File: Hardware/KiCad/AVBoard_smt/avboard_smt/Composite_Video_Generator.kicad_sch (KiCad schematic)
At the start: 47 parts, among them IC36 4040N, IC37 7430N, IC39 7400N, IC40 4040N, IC41 7400N, IC43 7400N, IC44 7486N, IC45 7400N, IC46 74257N, IC47 74257N, IC48 74564N, IC53 7404N, J2 VID_TO_MOBO, U2 THS7374

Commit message: update kicad SMT BOMs
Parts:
- V.RAM.0: MPN CONN SOCKET PLCC 68POS TIN -> 8468-21B1-RK-TR
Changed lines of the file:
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@@
       (effects (font (size 1.27 1.27)) hide)
     )
-    (property "MPN" "CONN SOCKET PLCC 68POS TIN" (at -330.2 154.94 0)
+    (property "MPN" "8468-21B1-RK-TR" (at -330.2 154.94 0)
       (effects (font (size 1.27 1.27)) hide)
     )
@@
       (effects (font (size 1.27 1.27)) hide)
     )
-    (property "MPN" "CONN SOCKET PLCC 68POS TIN" (at 106.68 132.08 0)
+    (property "MPN" "8468-21B1-RK-TR" (at 106.68 132.08 0)
       (effects (font (size 1.27 1.27)) hide)
     )
@@
       (effects (font (size 1.27 1.27)) hide)
     )
-    (property "MPN" "CONN SOCKET PLCC 68POS TIN" (at 314.96 172.72 0)
+    (property "MPN" "8468-21B1-RK-TR" (at 314.96 172.72 0)
       (effects (font (size 1.27 1.27)) hide)
     )
@@
       (effects (font (size 1.27 1.27)) hide)
     )
-    (property "MPN" "CONN SOCKET PLCC 68POS TIN" (at 88.9 332.74 0)
-      (effects (font (size 1.27 1.27)) hide)
-    )
+    (property "MPN" "8468-21B1-RK-TR" (at 88.9 332.74 0)
+      (effects (font (size 1.27 1.27)) hide)
+    )

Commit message: collect production documents for quoting
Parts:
- J2: footprint Connector_FFC-FPC:TE_4-1734839-0_1x40-1MP_P0.5mm_Horizontal -> SamacSys_Parts:F34G1A7Q1E8C40; MPN 4-1734839-0 -> F34G-1A7Q1-E8C40

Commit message: replace dual ported frame buffer with mirrored single ported rams
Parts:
- removed V.RAM.0: PDPRAM_32K_V2, Package_LCC:PLCC-68_SMD-Socket, symbol signals-eagle-import:PDPRAM_32K_V2
- added IC1, IC9: AS7C256A-10TIN, SOP55P1340X120-28N, symbol SamacSys_Parts:AS7C256A-10TIN
- added IC2_AUD0: 7432N, Package_SO:TSSOP-14_4.4x5mm_P0.65mm, symbol signals-eagle-import:7432N
- added U3, U4, U5: 74AHC373, Package_SO:TSSOP-20_4.4x6.5mm_P0.65mm, symbol 74xx:74AHC373
- added U6: 74AC00, Package_SO:TSSOP-14_4.4x5mm_P0.65mm, symbol 74xx:7400
- added U7: 74VHC74, Package_SO:TSSOP-14_4.4x5mm_P0.65mm, symbol 74xx:74HC74
- added U8, U9: 74HC244, Package_SO:TSSOP-20_4.4x6.5mm_P0.65mm, symbol 74xx:74HCT244
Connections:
- net CLK14: now also U7.2 (D)
- net CLK28: now also U7.11 (C), U7.3 (C)
- net CLK7: now also U6.1, U6.2
- net GND: now also IC1.21 (GND), IC1.27 (~{CE}), IC9.21 (GND), IC9.27 (~{CE}), U3.10 (GND), U4.10 (GND), U5.10 (GND), U6.7 (GND), U7.7 (GND), U8.10 (GND), U9.10 (GND)
- net P0: now also IC1.26 (I/O7), U3.19 (O7)
- net P1: now also IC1.25 (I/O6), U3.16 (O6)
- net P2: now also IC1.24 (I/O5), U3.15 (O5)
- net P3: now also IC1.23 (I/O4), U3.12 (O4)
- net P4: now also IC1.22 (I/O3), U3.9 (O3)
- net P5: now also IC1.20 (I/O2), U3.6 (O2)
- net P6: now also IC1.19 (I/O1), U3.5 (O1)
- net P7: now also IC1.18 (I/O0), U3.2 (O0)
- net VA0: now also IC9.17 (A0), U4.3 (D0)
- net VA1: now also IC9.16 (A1), U4.4 (D1)
- net VA10: now also IC9.28 (A10), U5.8 (D3)
- net VA11: now also IC9.2 (A11), U5.13 (D4)
- net VA12: now also IC9.9 (A12), U5.14 (D5)
- net VA13: now also IC9.5 (A13), U5.17 (D6)
- net VA14: now also IC9.8 (A14), U5.18 (D7)
- net VA2: now also IC9.15 (A2), U4.7 (D2)
- net VA3: now also IC9.14 (A3), U4.8 (D3)
- net VA4: now also IC9.13 (A4), U4.13 (D4)
- net VA5: now also IC9.12 (A5), U4.14 (D5)
- net VA6: now also IC9.11 (A6), U4.17 (D6)
- net VA7: now also IC9.10 (A7), U5.3 (D0)
- net VA8: now also IC9.4 (A8), U5.4 (D1)
- net VA9: now also IC9.3 (A9), U5.7 (D2)
- net VCC: now also IC1.7 (VCC), IC9.7 (VCC), U3.20 (VCC), U4.20 (VCC), U5.20 (VCC), U6.14 (VCC), U7.1 (~{R}), U7.10 (~{S}), U7.13 (~{R}), U7.14 (VCC), U7.4 (~{S}), U8.20 (VCC), U9.20 (VCC)
- net VD0: now also IC9.18 (I/O0), U3.3 (D0)
- net VD1: now also IC9.19 (I/O1), U3.4 (D1)
- net VD2: now also IC9.20 (I/O2), U3.7 (D2)
- net VD3: now also IC9.22 (I/O3), U3.8 (D3)
- net VD4: now also IC9.23 (I/O4), U3.13 (D4)
- net VD5: now also IC9.24 (I/O5), U3.14 (D5)
- net VD6: now also IC9.25 (I/O6), U3.17 (D6)
- net VD7: now also IC9.26 (I/O7), U3.18 (D7)
- net VIDPAGE: now also U9.11 (2A3)
- net XCLK: now also U6.4
- net ~{VOE}: now also IC9.1 (~{OE})
- net ~{VWE}: now also IC53.11 (I), IC9.6 (~{WE})
- net PIXLATCH: now reaches COL_CTR0.9 (Q1), IC48.11 (CLK)
- net PIXLATCH: now also U6.5, U7.12 (D)
- net PAY6: now reaches ROW_CTR0.4 (Q7)
- net PAY6: now also U9.13 (2A2)
- net PAY5: now reaches ROW_CTR0.2 (Q6)
- net PAY5: now also U9.15 (2A1)
- net PAY4: now reaches ROW_CTR0.3 (Q5)
- net PAY4: now also U9.17 (2A0)
- net PAY3: now reaches ROW_CTR0.5 (Q4)
- net PAY3: now also U9.8 (1A3)
- net PAY2: now reaches ROW_CTR0.6 (Q3)
- net PAY2: now also U9.6 (1A2)
- net PAY1: now reaches ROW_CTR0.7 (Q2)
- net PAY1: now also U9.4 (1A1)
- net PAY0: now reaches ROW_CTR0.9 (Q1)
- net PAY0: now also U9.2 (1A0)
- net PAX6: now reaches COL_CTR0.13 (Q8)
- net PAX6: now also U8.13 (2A2)
- net PAX5: now reaches COL_CTR0.4 (Q7)
- net PAX5: now also U8.15 (2A1)
- net PAX4: now reaches COL_CTR0.2 (Q6)
- net PAX4: now also U8.17 (2A0)
- net PAX3: now reaches COL_CTR0.3 (Q5)
- net PAX3: now also U8.8 (1A3)
- net PAX2: now reaches COL_CTR0.5 (Q4)
- net PAX2: now also U8.6 (1A2)
- net PAX1: now reaches COL_CTR0.6 (Q3)
- net PAX1: now also U8.4 (1A1)
- net PAX0: now reaches COL_CTR0.7 (Q2)
- net PAX0: now also U8.2 (1A0)
- new net: U6.10, U6.6, U6.9
- new net: IC1.1 (~{OE}), U7.9 (Q), U8.1 (1OE), U8.19 (2OE), U9.1 (1OE), U9.19 (2OE)
- new net: U6.12, U6.3
- new net: U6.13, U6.8
- new net LAG14: IC2_AUD0.12 (I0), U7.5 (Q)
- new net MA0: IC1.17 (A0), U4.2 (O0), U8.18 (1Y0)
- new net MA1: IC1.16 (A1), U4.5 (O1), U8.16 (1Y1)
- new net MA10: IC1.28 (A10), U5.9 (O3), U9.12 (1Y3)
- new net MA11: IC1.2 (A11), U5.12 (O4), U9.3 (2Y0)
- new net MA12: IC1.9 (A12), U5.15 (O5), U9.5 (2Y1)
- new net MA13: IC1.5 (A13), U5.16 (O6), U9.7 (2Y2)
- new net MA14: IC1.8 (A14), U5.19 (O7), U9.9 (2Y3)
- new net MA2: IC1.15 (A2), U4.6 (O2), U8.14 (1Y2)
- new net MA3: IC1.14 (A3), U4.9 (O3), U8.12 (1Y3)
- new net MA4: IC1.13 (A4), U4.12 (O4), U8.3 (2Y0)
- new net MA5: IC1.12 (A5), U4.15 (O5), U8.5 (2Y1)
- new net MA6: IC1.11 (A6), U4.16 (O6), U8.7 (2Y2)
- new net MA7: IC1.10 (A7), U5.2 (O0), U9.18 (1Y0)
- new net MA8: IC1.4 (A8), U5.5 (O1), U9.16 (1Y1)
- new net MA9: IC1.3 (A9), U5.6 (O2), U9.14 (1Y2)
- new net VWE: IC53.10 (O), U3.11 (LE), U4.11 (LE), U5.11 (LE)
- new net ~{MirrorLoad}: IC2_AUD0.13 (I1), U3.1 (OE), U4.1 (OE), U5.1 (OE), U6.11
- new net ~{MirrorWE}: IC1.6 (~{WE}), IC2_AUD0.11 (O)
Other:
- note added: "BLITSIDE FRAMEBUFFER"
- note added: "VIDSIDE FRAMEBUFFER MIRROR"
- moved on the sheet: COL_CTR0B, IC36B, IC40B, IC53E, ROW_CTR0B

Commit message: design out the 4K dualport ram
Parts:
- IC1, IC9: MPN (none) -> AS7C256A-10TIN; Manufacturer_Part_Number AS7C256A-10TIN -> (none)
- U3, U4, U5: MPN (none) -> 74VHC373MTCX

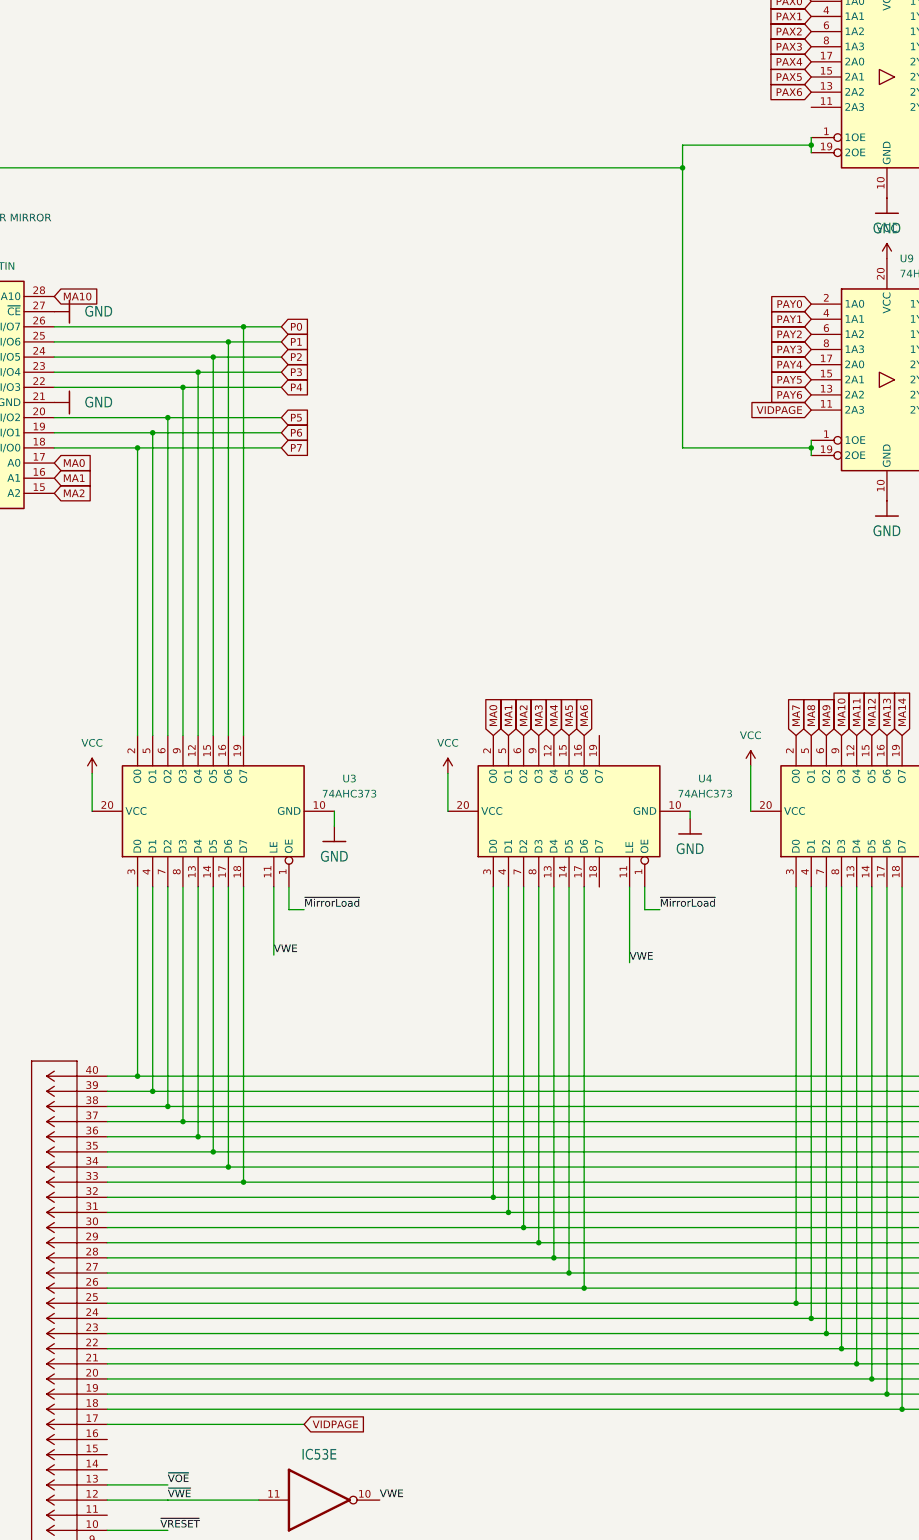
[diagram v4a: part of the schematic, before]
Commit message: connect loose unused inputs to ground
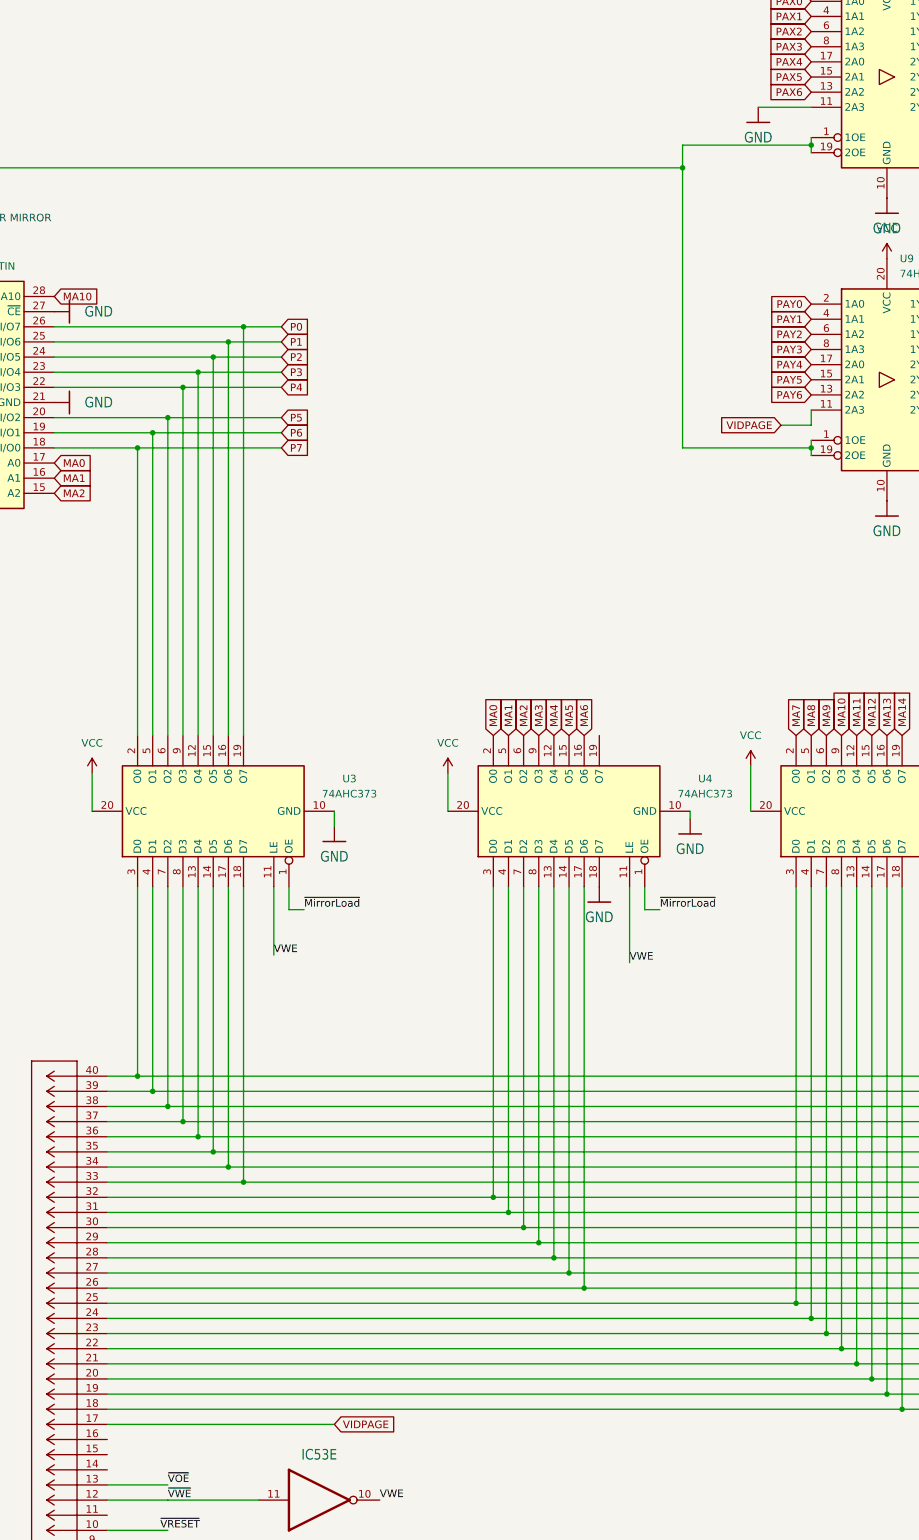
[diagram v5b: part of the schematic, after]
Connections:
- net GND: now also U4.18 (D7), U8.11 (2A3)

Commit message: fix composite video generator board
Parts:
- removed IC2_AUD0: 7432N, Package_SO:TSSOP-14_4.4x5mm_P0.65mm, symbol signals-eagle-import:7432N
- removed U6: 74AC00, Package_SO:TSSOP-14_4.4x5mm_P0.65mm, symbol 74xx:7400
- removed U7: 74VHC74, Package_SO:TSSOP-14_4.4x5mm_P0.65mm, symbol 74xx:74HC74
- added unit 1 of IC53
- added MIRROR_OR: 7432N, Package_SO:TSSOP-14_4.4x5mm_P0.65mm, symbol signals-eagle-import:7432N
- added PIX_CLK_DELAY: 74164N, Package_SO:TSSOP-14_4.4x5mm_P0.65mm, symbol signals-eagle-import:74164N
- SCAN_DELAY0, X_SCALER0: MPN MC74HC161ADTR2G -> SN74HC161PWR
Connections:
- net CLK14: now also MIRROR_OR.1 (I0)
- net CLK28: now also PIX_CLK_DELAY.8 (CLK)
- net GND: now also MIRROR_OR.7 (GND), PIX_CLK_DELAY.7 (GND)
- net P0: now also IC1.18 (I/O0), U3.2 (O0); no longer IC1.26 (I/O7), U3.19 (O7)
- net P1: now also IC1.19 (I/O1), U3.5 (O1); no longer IC1.25 (I/O6), U3.16 (O6)
- net P2: now also IC1.20 (I/O2), U3.6 (O2); no longer IC1.24 (I/O5), U3.15 (O5)
- net P3: now also IC1.22 (I/O3), U3.9 (O3); no longer IC1.23 (I/O4), U3.12 (O4)
- net P4: now also IC1.23 (I/O4), U3.12 (O4); no longer IC1.22 (I/O3), U3.9 (O3)
- net P5: now also IC1.24 (I/O5), U3.15 (O5); no longer IC1.20 (I/O2), U3.6 (O2)
- net P6: now also IC1.25 (I/O6), U3.16 (O6); no longer IC1.19 (I/O1), U3.5 (O1)
- net P7: now also IC1.26 (I/O7), U3.19 (O7); no longer IC1.18 (I/O0), U3.2 (O0)
- net PIXLATCH: now also PIX_CLK_DELAY.10 (QE); no longer COL_CTR0.9 (Q1)
- net VCC: now also MIRROR_OR.14 (VCC), PIX_CLK_DELAY.14 (VCC), PIX_CLK_DELAY.2 (B), PIX_CLK_DELAY.9 (CLR)
- net XCLK: now also IC53.2 (O); no longer IC53.2 (O)
- net ~{MirrorLoad}: now also MIRROR_OR.2 (I1), MIRROR_OR.6 (O)
- net ~{MirrorWE}: now also MIRROR_OR.3 (O)
- net at X_SCALER0.15 (RCO): now also IC53.1 (I); no longer IC53.1 (I)
- net ROW_COMPLETE: now reaches COL_CTR0.12 (Q9), IC53.3 (I)
- net ~{PIXLOAD}: now reaches IC1.1 (~{OE}), U8.1 (1OE), U8.19 (2OE), U9.1 (1OE), U9.19 (2OE)
- net ~{PIXLOAD}: now also IC53.12 (O)
- new net PIXCLK: COL_CTR0.9 (Q1), MIRROR_OR.4 (I0), PIX_CLK_DELAY.1 (A)
- new net PIXCLK_PhaseC: MIRROR_OR.5 (I1), PIX_CLK_DELAY.5 (QC)
- new net PIXLOAD: IC53.13 (I), PIX_CLK_DELAY.3 (QA)
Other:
- note removed: "YOU ALREADY FIXED THIS STOP MESSING WITH IT"

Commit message: Add AV board version with VRAM replaced but not ARAM
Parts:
- added unit 1 of IC53
- added unit 1 of MIRROR_OR1
- added unit 2 of MIRROR_OR1
- added unit 1 of PIX_CLK_DELAY1
- added TP1: Sync, TestPoint:TestPoint_Pad_D3.0mm, symbol Connector:TestPoint
- added TP2: Luma, TestPoint:TestPoint_Pad_D3.0mm, symbol Connector:TestPoint
- added TP3: Chroma, TestPoint:TestPoint_Pad_D3.0mm, symbol Connector:TestPoint
- renumbered MIRROR_OR to MIRROR_OR1, PIX_CLK_DELAY to PIX_CLK_DELAY1
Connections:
- net CHROMACARRIER: now also TP3.1
- net CLK14: now also MIRROR_OR1.1 (I0); no longer MIRROR_OR1.1 (I0)
- net CLK28: now also PIX_CLK_DELAY1.8 (CLK); no longer PIX_CLK_DELAY1.8 (CLK)
- net CSYNC: now also TP1.1
- net LUMA: now also TP2.1
- net PIXCLK: now also MIRROR_OR1.4 (I0), PIX_CLK_DELAY1.1 (A); no longer MIRROR_OR1.4 (I0), PIX_CLK_DELAY1.1 (A)
- net PIXCLK_PhaseC: now also MIRROR_OR1.5 (I1), PIX_CLK_DELAY1.5 (QC); no longer MIRROR_OR1.5 (I1), PIX_CLK_DELAY1.5 (QC)
- net PIXLATCH: now also PIX_CLK_DELAY1.10 (QE); no longer PIX_CLK_DELAY1.10 (QE)
- net PIXLOAD: now also PIX_CLK_DELAY1.3 (QA); no longer PIX_CLK_DELAY1.3 (QA)
- net VCC: now also PIX_CLK_DELAY1.2 (B), PIX_CLK_DELAY1.9 (CLR); no longer PIX_CLK_DELAY1.2 (B), PIX_CLK_DELAY1.9 (CLR)
- net XCLK: now also IC53.2 (O); no longer IC53.2 (O)
- net ~{MirrorLoad}: now also MIRROR_OR1.2 (I1), MIRROR_OR1.6 (O); no longer MIRROR_OR1.2 (I1), MIRROR_OR1.6 (O)
- net ~{MirrorWE}: now also MIRROR_OR1.3 (O); no longer MIRROR_OR1.3 (O)
- net at X_SCALER0.15 (RCO): now also IC53.1 (I); no longer IC53.1 (I)

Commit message: updates
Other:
- moved on the sheet: COL_CTR0A, COL_CTR0B, HBLANK_LATCH0A, HBLANK_LATCH0B, IC1, IC36A, IC36B, IC37A, IC39A, IC39B, IC39C, IC39D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
